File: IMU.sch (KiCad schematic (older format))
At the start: 6 parts, among them U12 MPU-9250

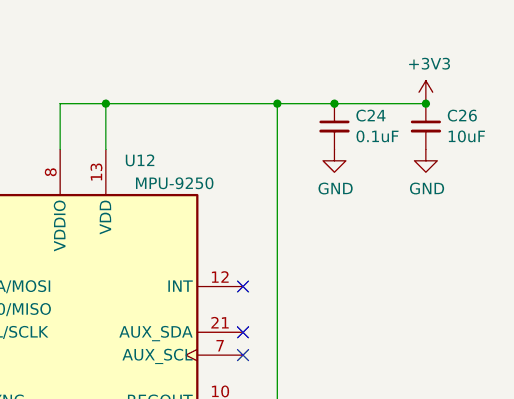
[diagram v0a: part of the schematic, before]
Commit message: Updated BT module connection, 3D models and wiring.
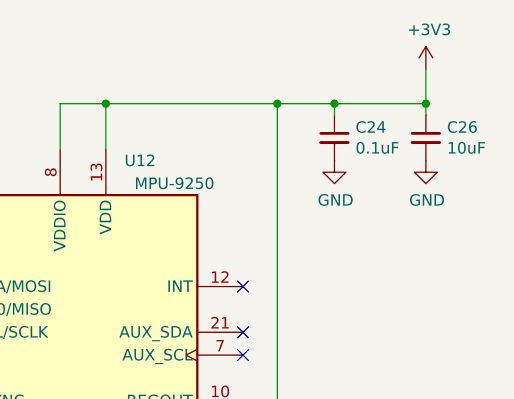
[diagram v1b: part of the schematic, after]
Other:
- moved on the sheet: C24, C26
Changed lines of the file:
@@
 L power:+3V3 #PWR?
 U 1 1 5E6F367E
-P 7200 2700
+P 7200 2550
 AR Path="/5E5F55D4/5E6F367E" Ref="#PWR?"  Part="1"
 AR Path="/5E6F1BD7/5E6F367E" Ref="#PWR0174"  Part="1"
-F 0 "#PWR0174" H 7200 2550 50  0001 C CNN
-F 1 "+3V3" H 7215 2873 50  0000 C CNN
-F 2 "" H 7200 2700 50  0001 C CNN
-F 3 "" H 7200 2700 50  0001 C CNN
-	1    7200 2700
+F 0 "#PWR0174" H 7200 2400 50  0001 C CNN
+F 1 "+3V3" H 7215 2723 50  0000 C CNN
+F 2 "" H 7200 2550 50  0001 C CNN
+F 3 "" H 7200 2550 50  0001 C CNN
+	1    7200 2550
 	1    0    0    -1
 $EndComp
@@
 L Device:C_Small C?
 U 1 1 5E6F3684
-P 6800 2800
+P 6800 2850
 AR Path="/5E5F55D4/5E6F3684" Ref="C?"  Part="1"
 AR Path="/5E6F1BD7/5E6F3684" Ref="C24"  Part="1"
-F 0 "C24" H 6892 2846 50  0000 L CNN
-F 1 "0.1uF" H 6892 2755 50  0000 L CNN
-F 2 "Capacitor_SMD:C_0402_1005Metric" H 6800 2800 50  0001 C CNN
-F 3 "~" H 6800 2800 50  0001 C CNN
-	1    6800 2800
+F 0 "C24" H 6892 2896 50  0000 L CNN
+F 1 "0.1uF" H 6892 2805 50  0000 L CNN
+F 2 "Capacitor_SMD:C_0402_1005Metric" H 6800 2850 50  0001 C CNN
+F 3 "~" H 6800 2850 50  0001 C CNN
+	1    6800 2850
 	1    0    0    -1
 $EndComp
@@
 Wire Wire Line
 	5600 2700 5600 2900
-Connection ~ 6800 2700
 Wire Wire Line
 	5800 2900 5800 2700
@@
 L power:GND #PWR?
 U 1 1 5E6F369C
-P 7200 2900
+P 7200 2950
 AR Path="/5E5F55D4/5E6F369C" Ref="#PWR?"  Part="1"
 AR Path="/5E6F1BD7/5E6F369C" Ref="#PWR0176"  Part="1"
-F 0 "#PWR0176" H 7200 2650 50  0001 C CNN
-F 1 "GND" H 7205 2727 50  0000 C CNN
-F 2 "" H 7200 2900 50  0001 C CNN
-F 3 "" H 7200 2900 50  0001 C CNN
-	1    7200 2900
+F 0 "#PWR0176" H 7200 2700 50  0001 C CNN
+F 1 "GND" H 7205 2777 50  0000 C CNN
+F 2 "" H 7200 2950 50  0001 C CNN
+F 3 "" H 7200 2950 50  0001 C CNN
+	1    7200 2950
 	1    0    0    -1
 $EndComp
@@
 L Device:C_Small C?
 U 1 1 5E6F36BE
-P 7200 2800
+P 7200 2850
 AR Path="/5E5F55D4/5E6F36BE" Ref="C?"  Part="1"
 AR Path="/5E6F1BD7/5E6F36BE" Ref="C26"  Part="1"
-F 0 "C26" H 7292 2846 50  0000 L CNN
-F 1 "10uF" H 7292 2755 50  0000 L CNN
-F 2 "Capacitor_SMD:C_0603_1608Metric" H 7200 2800 50  0001 C CNN
-F 3 "~" H 7200 2800 50  0001 C CNN
-	1    7200 2800
+F 0 "C26" H 7292 2896 50  0000 L CNN
+F 1 "10uF" H 7292 2805 50  0000 L CNN
+F 2 "Capacitor_SMD:C_0603_1608Metric" H 7200 2850 50  0001 C CNN
+F 3 "~" H 7200 2850 50  0001 C CNN
+	1    7200 2850
 	1    0    0    -1
 $EndComp
@@
 L power:GND #PWR?
 U 1 1 5E6F36C4
-P 6800 2900
+P 6800 2950
 AR Path="/5E5F55D4/5E6F36C4" Ref="#PWR?"  Part="1"
 AR Path="/5E6F1BD7/5E6F36C4" Ref="#PWR0179"  Part="1"
-F 0 "#PWR0179" H 6800 2650 50  0001 C CNN
-F 1 "GND" H 6805 2727 50  0000 C CNN
-F 2 "" H 6800 2900 50  0001 C CNN
-F 3 "" H 6800 2900 50  0001 C CNN
-	1    6800 2900
-	1    0    0    -1
-$EndComp
-Wire Wire Line
-	6800 2700 7200 2700
-Connection ~ 7200 2700
+F 0 "#PWR0179" H 6800 2700 50  0001 C CNN
+F 1 "GND" H 6805 2777 50  0000 C CNN
+F 2 "" H 6800 2950 50  0001 C CNN
+F 3 "" H 6800 2950 50  0001 C CNN
+	1    6800 2950
+	1    0    0    -1
+$EndComp
 Wire Wire Line
 	5000 3600 4850 3600
@@
 Connection ~ 6550 2700
 Wire Wire Line
+	7200 2700 7200 2550
+Wire Wire Line
 	6550 2700 6800 2700
+Wire Wire Line
+	6800 2750 6800 2700
+Connection ~ 6800 2700
+Wire Wire Line
+	6800 2700 7200 2700
+Wire Wire Line
+	7200 2750 7200 2700
+Connection ~ 7200 2700
 $EndSCHEMATC
